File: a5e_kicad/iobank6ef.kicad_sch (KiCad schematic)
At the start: 1 part, among them U7 A5EB013B-B23B

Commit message: Schematic reorg step 1: remove dangling stubs and stale notes, correct notes, fill title blocks
Netlist: 0 renamed, 0 connectivity diffs; DRC parity 0. ERC 315 -> 242.
Plan refreshed for the eMMC, RTL8211FDI, TPS548A28 and the tuned LPDDR4 (IOBANK 3 sheet name kept).
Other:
- title: (none) -> Banks 6E / 6F HVIO
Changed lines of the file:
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@@
 	(paper "A4")
 	(title_block
-		(rev "0.1")
+		(title "Banks 6E / 6F HVIO")
+		(rev "${REVISION}")
+		(comment 1 "${BOARD}")
 	)
 	(no_connect

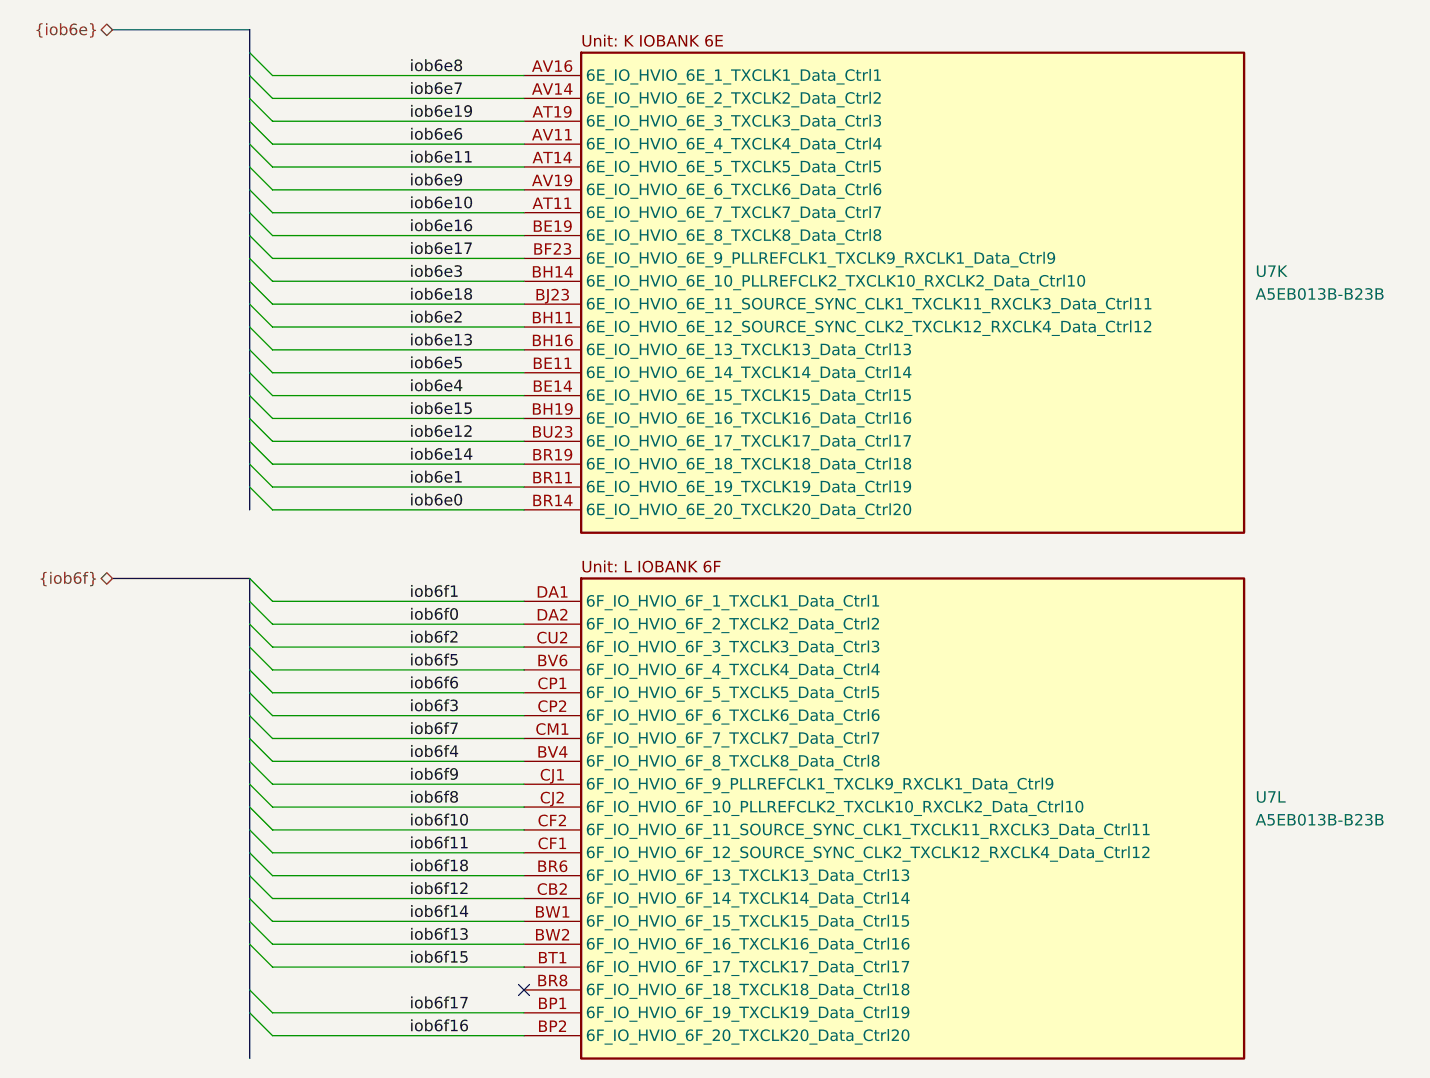
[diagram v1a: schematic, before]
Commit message: Schematic reorg step 7: no global labels, NC flags on unused U7 pins
- hps_uart0_tx/rx, eth_rst_n, phy_rst_n, fpga_led: global labels replaced by
  sheet pins; eth_led_g_n is a local label
- HyperBus labels/bus, the HPS {hps_i2c} bus and the pwr_scl/pwr_sda wiring
  removed (nothing behind them)
- 118 U7 pins that only had a net label: label, stub and bus entry removed,
  no-connect flag added
- Bank 3A notes restacked
- PCB: 124 nets renamed (118 to unconnected-(U7...))

Netdiff: 124 renamed, 0 connectivity diffs. ERC 148 -> 21. DRC parity 0.
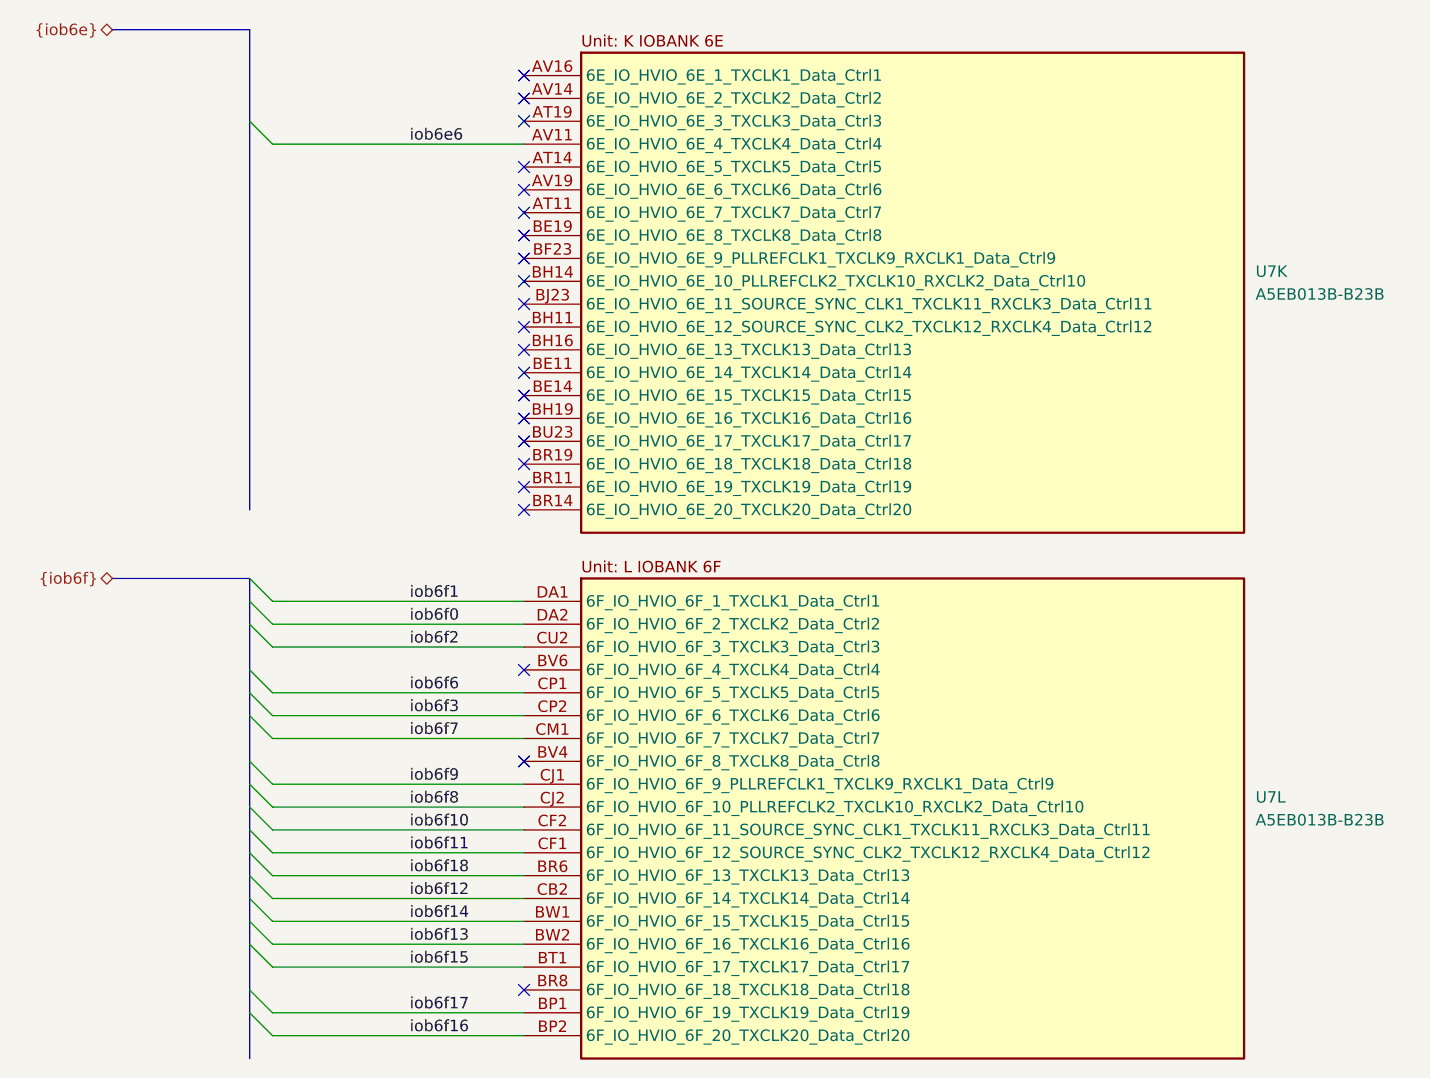
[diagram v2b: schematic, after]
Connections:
- net iob6e0: no longer names the net of U7.BR14 (6E_IO_HVIO_6E_20_TXCLK20_Data_Ctrl20)
- net iob6e1: no longer names the net of U7.BR11 (6E_IO_HVIO_6E_19_TXCLK19_Data_Ctrl19)
- net iob6e10: no longer names the net of U7.AT11 (6E_IO_HVIO_6E_7_TXCLK7_Data_Ctrl7)
- net iob6e11: no longer names the net of U7.AT14 (6E_IO_HVIO_6E_5_TXCLK5_Data_Ctrl5)
- net iob6e12: no longer names the net of U7.BU23 (6E_IO_HVIO_6E_17_TXCLK17_Data_Ctrl17)
- net iob6e13: no longer names the net of U7.BH16 (6E_IO_HVIO_6E_13_TXCLK13_Data_Ctrl13)
- net iob6e14: no longer names the net of U7.BR19 (6E_IO_HVIO_6E_18_TXCLK18_Data_Ctrl18)
- net iob6e15: no longer names the net of U7.BH19 (6E_IO_HVIO_6E_16_TXCLK16_Data_Ctrl16)
- net iob6e16: no longer names the net of U7.BE19 (6E_IO_HVIO_6E_8_TXCLK8_Data_Ctrl8)
- net iob6e17: no longer names the net of U7.BF23 (6E_IO_HVIO_6E_9_PLLREFCLK1_TXCLK9_RXCLK1_Data_Ctrl9)
- net iob6e18: no longer names the net of U7.BJ23 (6E_IO_HVIO_6E_11_SOURCE_SYNC_CLK1_TXCLK11_RXCLK3_Data_Ctrl11)
- net iob6e19: no longer names the net of U7.AT19 (6E_IO_HVIO_6E_3_TXCLK3_Data_Ctrl3)
- net iob6e2: no longer names the net of U7.BH11 (6E_IO_HVIO_6E_12_SOURCE_SYNC_CLK2_TXCLK12_RXCLK4_Data_Ctrl12)
- net iob6e3: no longer names the net of U7.BH14 (6E_IO_HVIO_6E_10_PLLREFCLK2_TXCLK10_RXCLK2_Data_Ctrl10)
- net iob6e4: no longer names the net of U7.BE14 (6E_IO_HVIO_6E_15_TXCLK15_Data_Ctrl15)
- net iob6e5: no longer names the net of U7.BE11 (6E_IO_HVIO_6E_14_TXCLK14_Data_Ctrl14)
- net iob6e7: no longer names the net of U7.AV14 (6E_IO_HVIO_6E_2_TXCLK2_Data_Ctrl2)
- net iob6e8: no longer names the net of U7.AV16 (6E_IO_HVIO_6E_1_TXCLK1_Data_Ctrl1)
- net iob6e9: no longer names the net of U7.AV19 (6E_IO_HVIO_6E_6_TXCLK6_Data_Ctrl6)
- net iob6f4: no longer names the net of U7.BV4 (6F_IO_HVIO_6F_8_TXCLK8_Data_Ctrl8)
- net iob6f5: no longer names the net of U7.BV6 (6F_IO_HVIO_6F_4_TXCLK4_Data_Ctrl4)
- no-connect marks 1 -> 22
